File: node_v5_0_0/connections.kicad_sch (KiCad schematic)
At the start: 15 parts, among them J1 Conn_01x02_Pin, J2 U.FL, J3 Conn_Coaxial, J4 Conn_02x08_Odd_Even, J5 Conn_02x02_Odd_Even, J6 U.FL, J8 Conn_01x02_Pin, J9 U.FL

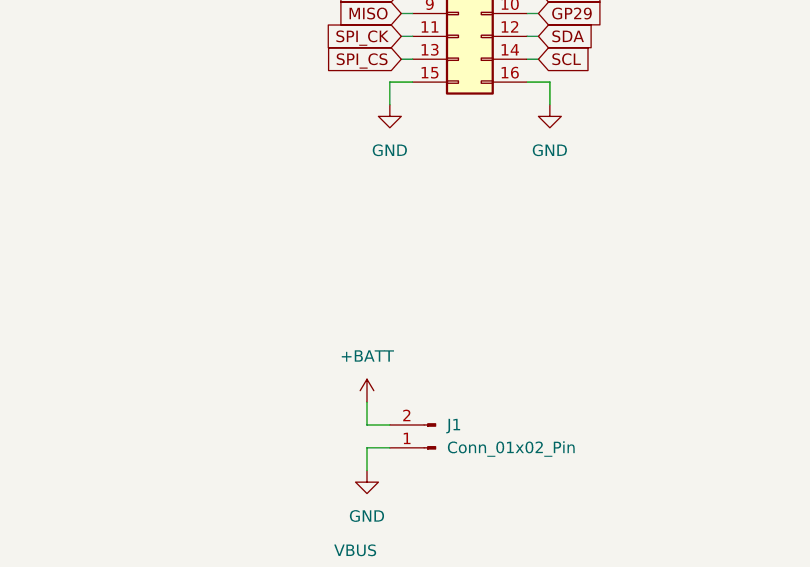
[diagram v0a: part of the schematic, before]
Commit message: updated layout
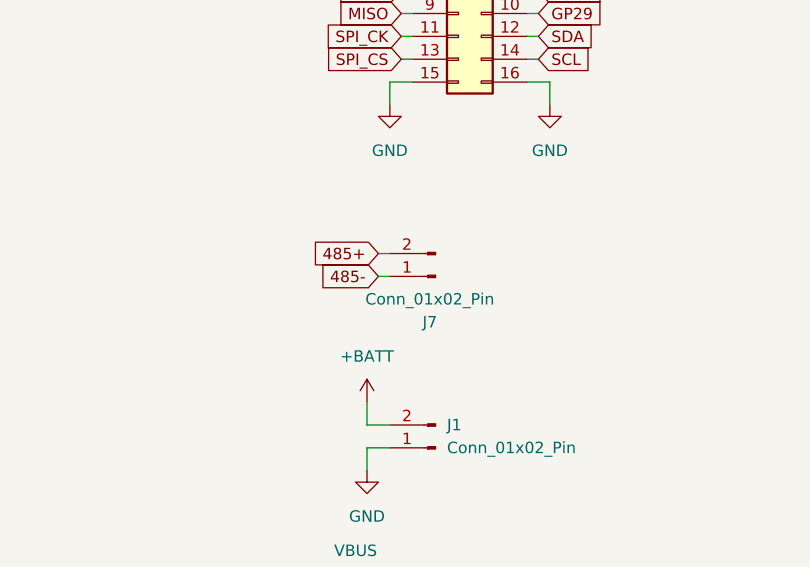
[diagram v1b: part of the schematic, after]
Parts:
- added J7: Conn_01x02_Pin, Connector_PinHeader_2.54mm:PinHeader_1x02_P2.54mm_Vertical, symbol Connector:Conn_01x02_Pin
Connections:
- new net 485+: J7.2 (Pin_2)
- new net 485-: J7.1 (Pin_1)
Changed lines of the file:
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@@
+	(wire
+		(pts
+			(xy 102.87 129.54) (xy 104.14 129.54)
+		)
+		(stroke
+			(width 0)
+			(type default)
+		)
+	)
 	(wire
 		(pts
@@
 	(wire
 		(pts
+			(xy 102.87 132.08) (xy 104.14 132.08)
+		)
+		(stroke
+			(width 0)
+			(type default)
+		)
+	)
+	(wire
+		(pts
 			(xy 261.62 74.93) (xy 261.62 77.47)
 		)
@@
 		)
 	)
+	(global_label "485+"
+		(shape input)
+		(at 102.87 129.54 180)
+		(fields_autoplaced yes)
+		(effects
+			(font
+				(size 1.27 1.27)
+			)
+			(justify right)
+		)
+		(property "Intersheetrefs" "${INTERSHEET_REFS}"
+			(at 94.6839 129.54 0)
+			(effects
+				(font
+					(size 1.27 1.27)
+				)
+				(justify right)
+				(hide yes)
+			)
+		)
+	)
 	(global_label "RX1"
 		(shape input)
@@
 				)
 				(justify left)
+				(hide yes)
+			)
+		)
+	)
+	(global_label "485-"
+		(shape input)
+		(at 102.87 132.08 180)
+		(fields_autoplaced yes)
+		(effects
+			(font
+				(size 1.27 1.27)
+			)
+			(justify right)
+		)
+		(property "Intersheetrefs" "${INTERSHEET_REFS}"
+			(at 94.6839 132.08 0)
+			(effects
+				(font
+					(size 1.27 1.27)
+				)
+				(justify right)
 				(hide yes)
 			)
@@
 					(unit 1)
 				)
+			)
+		)
+	)
+	(symbol
+		(lib_id "Connector:Conn_01x02_Pin")
+		(at 109.22 132.08 180)
+		(unit 1)
+		(exclude_from_sim no)
+		(in_bom yes)
+		(on_board yes)
+		(dnp no)
+		(fields_autoplaced yes)
+		(property "Reference" "J7"
+			(at 108.585 137.16 0)
+			(effects
+				(font
+					(size 1.27 1.27)
+				)
+			)
+		)
+		(property "Value" "Conn_01x02_Pin"
+			(at 108.585 134.62 0)
+			(effects
+				(font
+					(size 1.27 1.27)
+				)
+			)
+		)
+		(property "Footprint" "Connector_PinHeader_2.54mm:PinHeader_1x02_P2.54mm_Vertical"
+			(at 109.22 132.08 0)
+			(effects
+				(font
+					(size 1.27 1.27)
+				)
+				(hide yes)
+			)
+		)
+		(property "Datasheet" "~"
+			(at 109.22 132.08 0)
+			(effects
+				(font
+					(size 1.27 1.27)
+				)
+				(hide yes)
+			)
+		)
+		(property "Description" "Generic connector, single row, 01x02, script generated"
+			(at 109.22 132.08 0)
+			(effects
+				(font
+					(size 1.27 1.27)
+				)
+				(hide yes)
+			)
+		)
+		(pin "2"
+		)
+		(pin "1"
+		)
+		(instances
+			(project "node_v5_0_0"
+				(path "/03dc898e-8f05-4377-b5c6-8a0f09836da8/acf22234-ba16-4d6b-83f4-1166d3ac6600"
+					(reference "J7")
+					(unit 1)
+				)
